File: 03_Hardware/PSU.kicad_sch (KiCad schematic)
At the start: 1 part, among them U301 TPS54202DDC

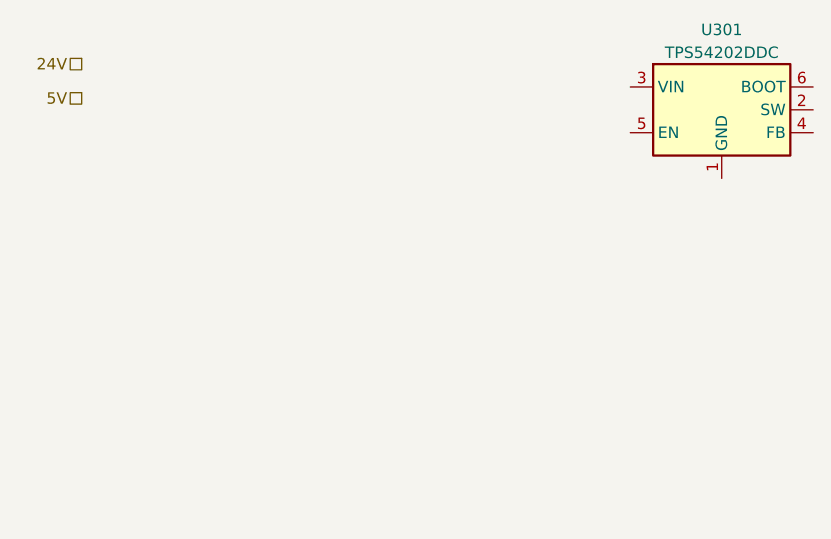
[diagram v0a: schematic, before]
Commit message: Schaltplan erweitert, I2C eingebaut
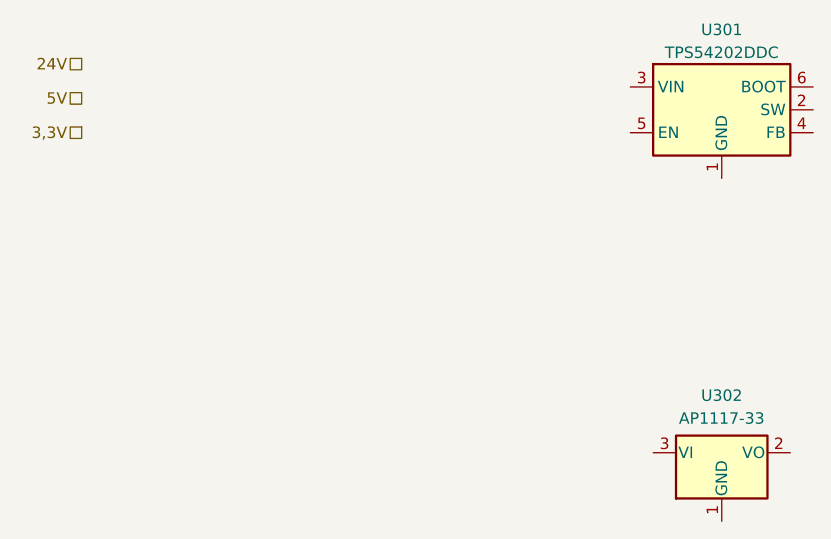
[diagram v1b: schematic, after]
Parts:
- added U302: AP1117-33, Package_TO_SOT_SMD:SOT-223-3_TabPin2, symbol Regulator_Linear:AP1117-33
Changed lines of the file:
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@@
+    (effects (font (size 1.27 1.27)) (justify right))
+  )
+  (hierarchical_label "3,3V" (shape passive) (at 55.88 71.12 180) (fields_autoplaced)
     (effects (font (size 1.27 1.27)) (justify right))
   )
@@
     (pin "6")
   )
+  (symbol (lib_id "Regulator_Linear:AP1117-33") (at 127 106.68 0) (unit 1)
+    (in_bom yes) (on_board yes) (dnp no) (fields_autoplaced)
+    (default_instance (reference "U302") (unit 1) (value "AP1117-33") (footprint "Package_TO_SOT_SMD:SOT-223-3_TabPin2"))
+    (property "Reference" "U302" (id 0) (at 127 100.33 0)
+      (effects (font (size 1.27 1.27)))
+    )
+    (property "Value" "AP1117-33" (id 1) (at 127 102.87 0)
+      (effects (font (size 1.27 1.27)))
+    )
+    (property "Footprint" "Package_TO_SOT_SMD:SOT-223-3_TabPin2" (id 2) (at 127 101.6 0)
+      (effects (font (size 1.27 1.27)) hide)
+    )
+    (property "Datasheet" "http://www.diodes.com/datasheets/AP1117.pdf" (id 3) (at 129.54 113.03 0)
+      (effects (font (size 1.27 1.27)) hide)
+    )
+    (pin "1")
+    (pin "2")
+    (pin "3")
+  )
 )

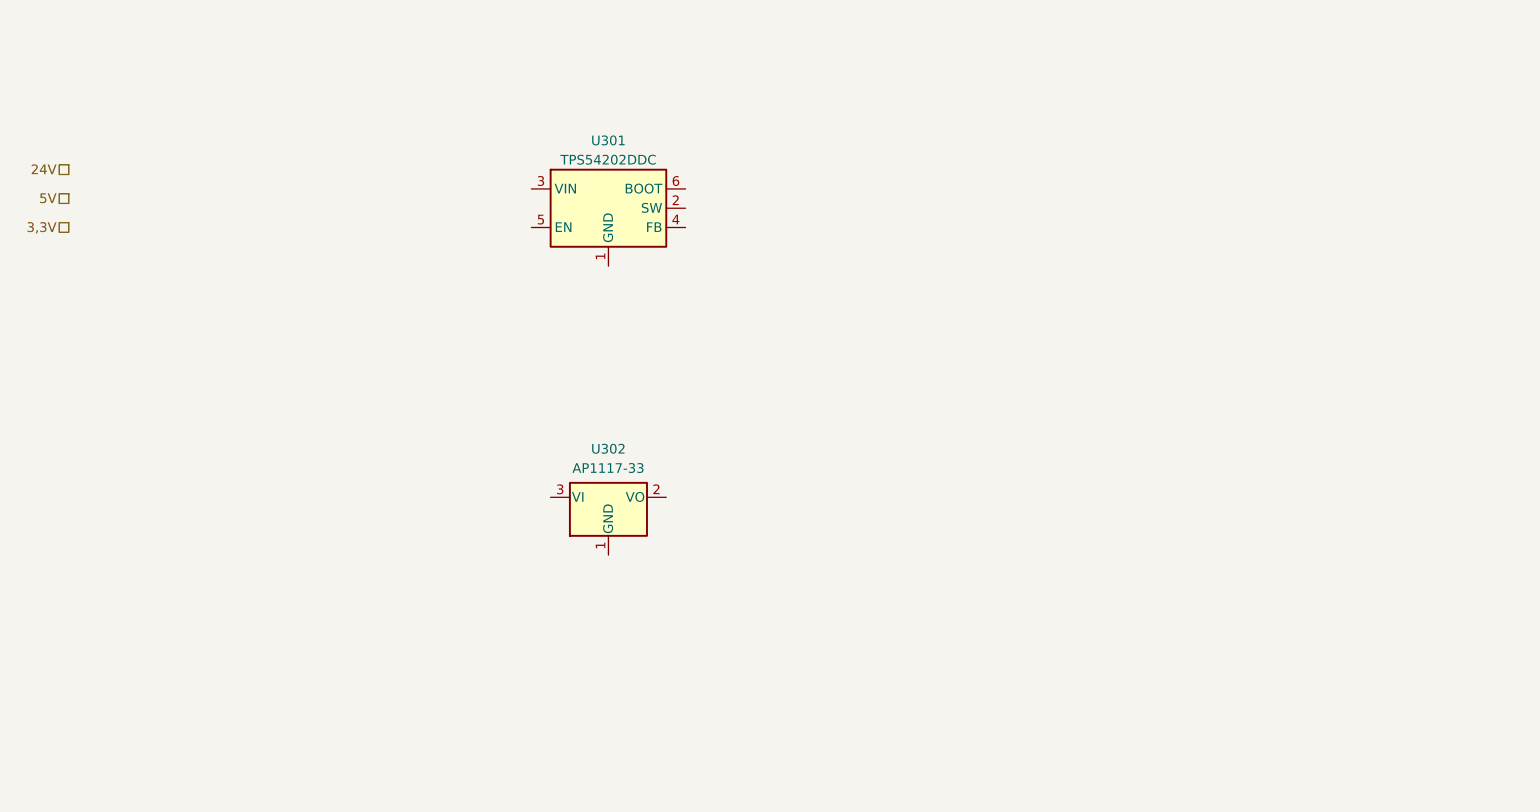
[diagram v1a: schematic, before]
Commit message: Schaltwandler für 5V und Linearwandler für 3,3V angelegt
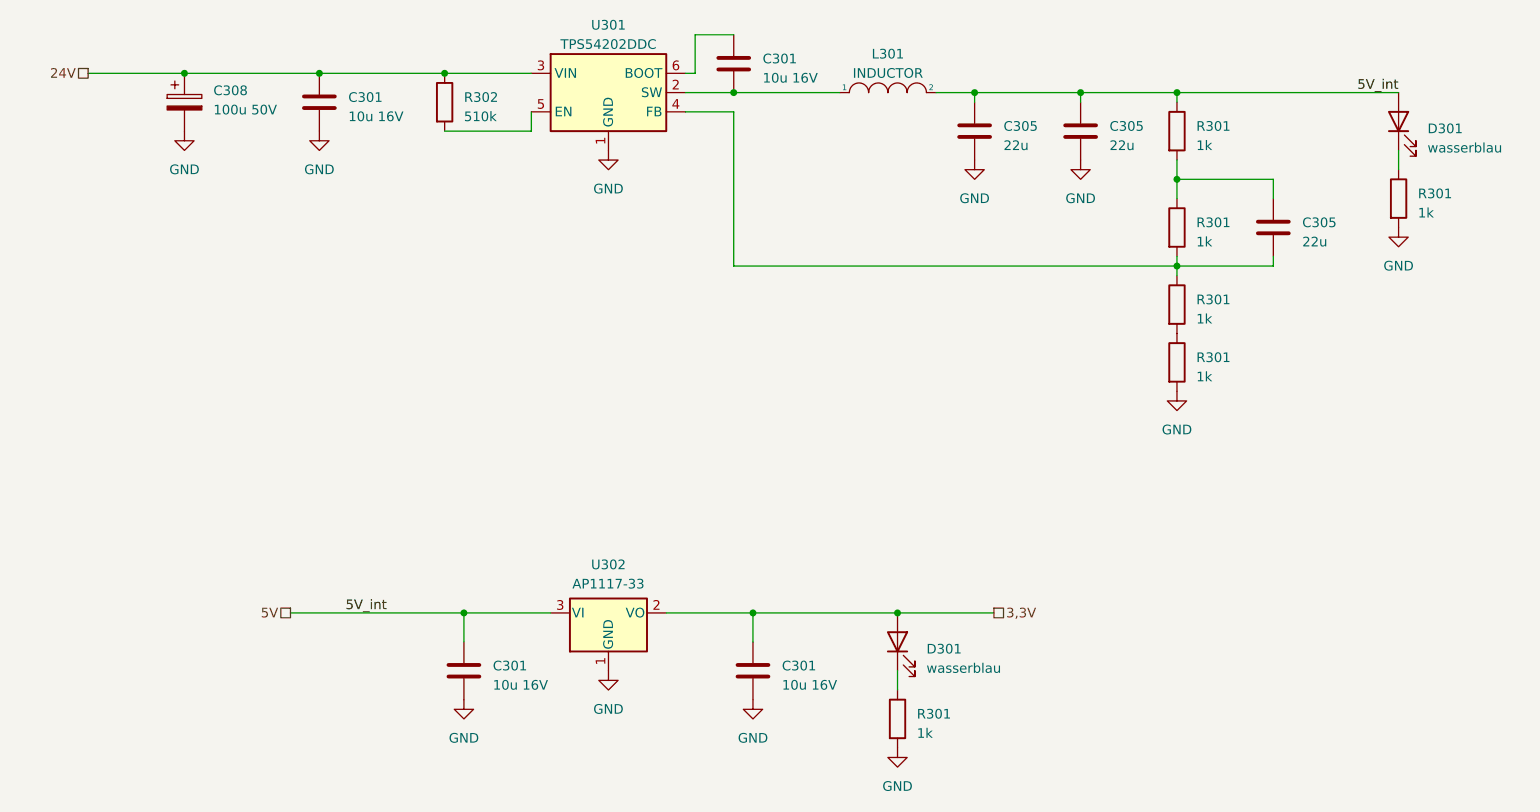
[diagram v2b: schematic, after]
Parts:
- added C301 (x4): 10u 16V, symbol Device:C
- added C305 (x3): 22u, symbol Device:C
- added C308: 100u 50V, symbol Device:C_Polarized
- added D301 (x2): wasserblau, symbol Device:LED
- added L301: INDUCTOR, symbol pspice:INDUCTOR
- added R301 (x6): 1k, symbol Device:R
- added R302: 510k, symbol Device:R
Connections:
- net 24V: now also U301.3 (VIN), C301.1, C308.1, R302.1
- net 3,3V: now also U302.2 (VO), C301.1, D301.2 (A)
- net 5V: now also U302.3 (VI), C301.1, C305.1, C305.1, D301.2 (A), L301.2, R301.1
- net GND: now reaches U301.1 (GND)
- net GND: now also U302.1 (GND), C301.2, C301.2, C301.2, C305.2, C305.2, C308.2, R301.2, R301.2, R301.2
- net at U301.2 (SW): now also C301.2, L301.1
- net at U301.4 (FB): now also C305.2, R301.1, R301.2
- net at U301.5 (EN): now also R302.2
- net at U301.6 (BOOT): now also C301.1
- new net: D301.1 (K), R301.1 (x2)
- new net: R301.1, R301.2
- new net: C305.1, R301.1, R301.2
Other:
- title: Stromversorgung der 5V-Komponenten -> Stromversorgung der 5V und 3,3V-Komponenten
- moved on the sheet: U301, U302

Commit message: Versionsänderungen 6.99 auf 7.0rc, Übergang alte Version 1 auf Version 2.dev
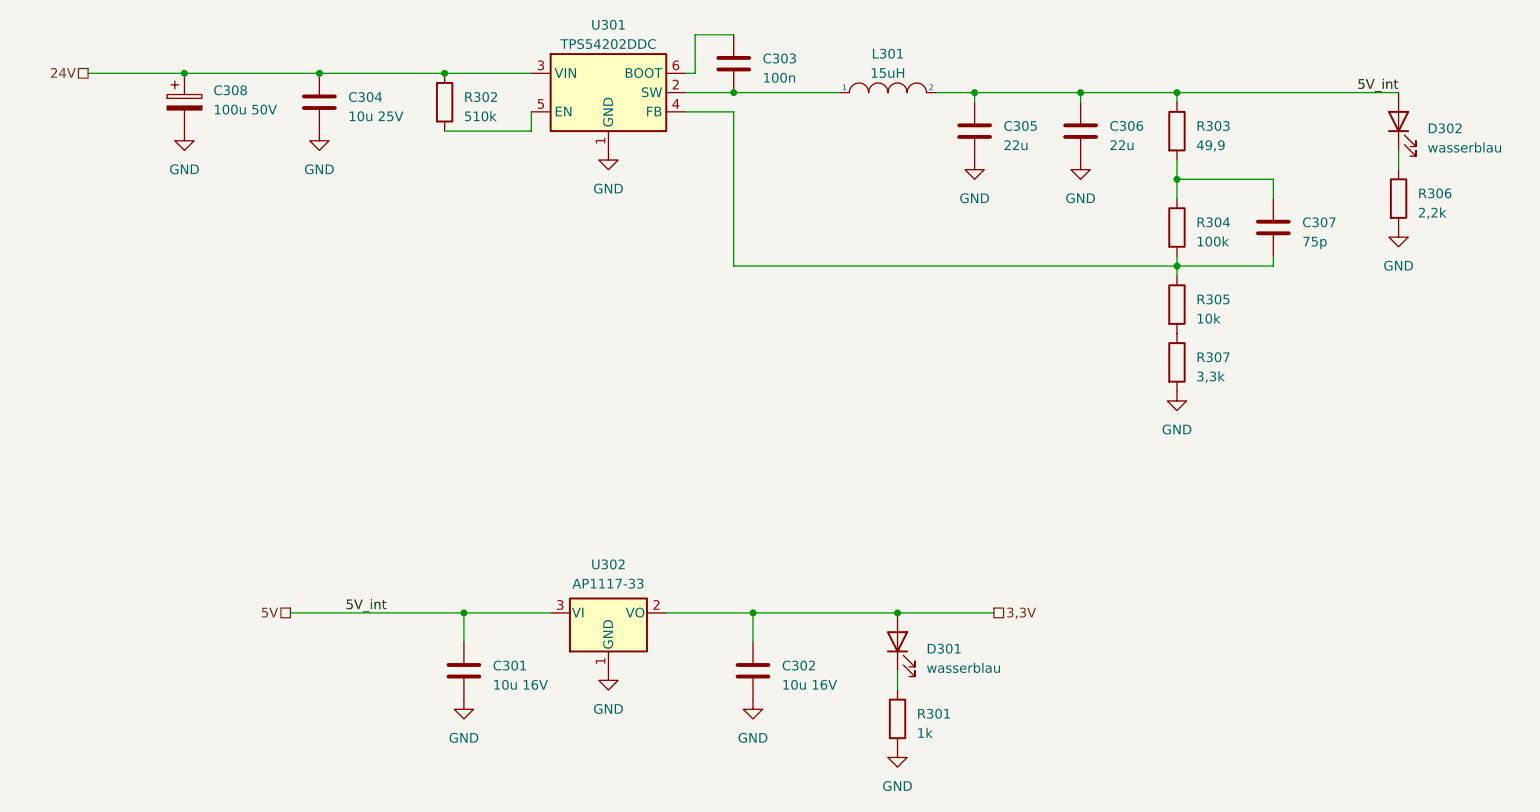
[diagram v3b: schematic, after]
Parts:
- C301, C305: footprint (none) -> Capacitor_SMD:C_1206_3216Metric
- C302: renamed from C301; footprint (none) -> Capacitor_SMD:C_1206_3216Metric
- C303: renamed from C301; value 10u 16V -> 100n; footprint (none) -> Capacitor_SMD:C_0603_1608Metric
- C304: renamed from C301; value 10u 16V -> 10u 25V; footprint (none) -> Capacitor_SMD:C_1206_3216Metric
- C306: renamed from C305; footprint (none) -> Capacitor_SMD:C_1206_3216Metric
- C307: renamed from C305; value 22u -> 75p; footprint (none) -> Capacitor_SMD:C_0603_1608Metric
- C308: footprint (none) -> Capacitor_THT:CP_Radial_D8.0mm_P3.50mm
- D301: footprint (none) -> LED_SMD:LED_0603_1608Metric
- D302: renamed from D301; footprint (none) -> LED_SMD:LED_0603_1608Metric
- L301: value INDUCTOR -> 15uH; footprint (none) -> Inductor_SMD:L_Bourns-SRN4018
- R301, R302: footprint (none) -> Resistor_SMD:R_0603_1608Metric
- R303: renamed from R301; value 1k -> 49,9; footprint (none) -> Resistor_SMD:R_0603_1608Metric
- R304: renamed from R301; value 1k -> 100k; footprint (none) -> Resistor_SMD:R_0603_1608Metric
- R305: renamed from R301; value 1k -> 10k; footprint (none) -> Resistor_SMD:R_0603_1608Metric
- R306: renamed from R301; value 1k -> 2,2k; footprint (none) -> Resistor_SMD:R_0603_1608Metric
- R307: renamed from R301; value 1k -> 3,3k; footprint (none) -> Resistor_SMD:R_0603_1608Metric

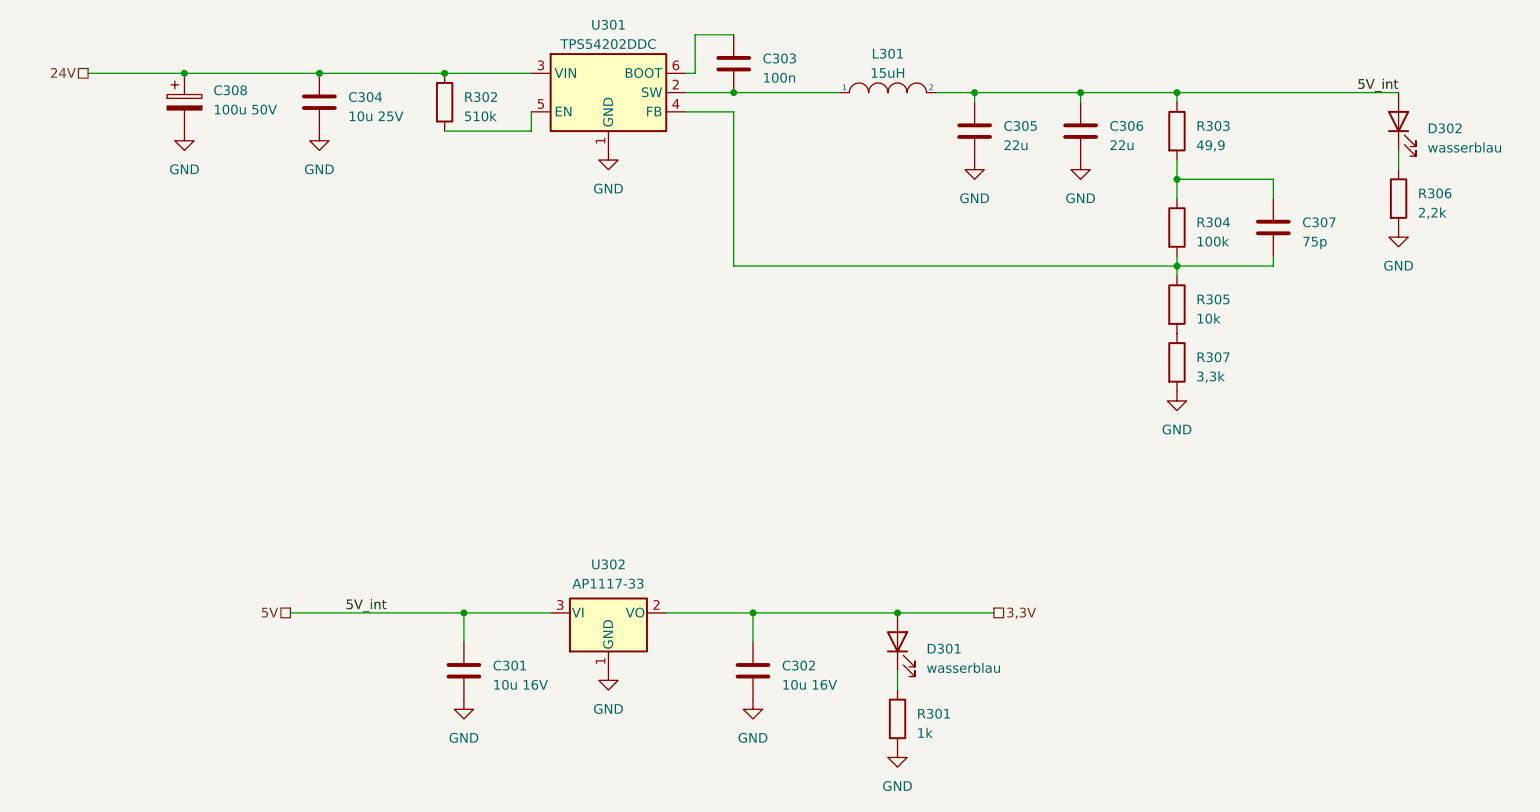
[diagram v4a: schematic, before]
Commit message: Stecker fertig ausgewählt und Layout etwa 60% fertig
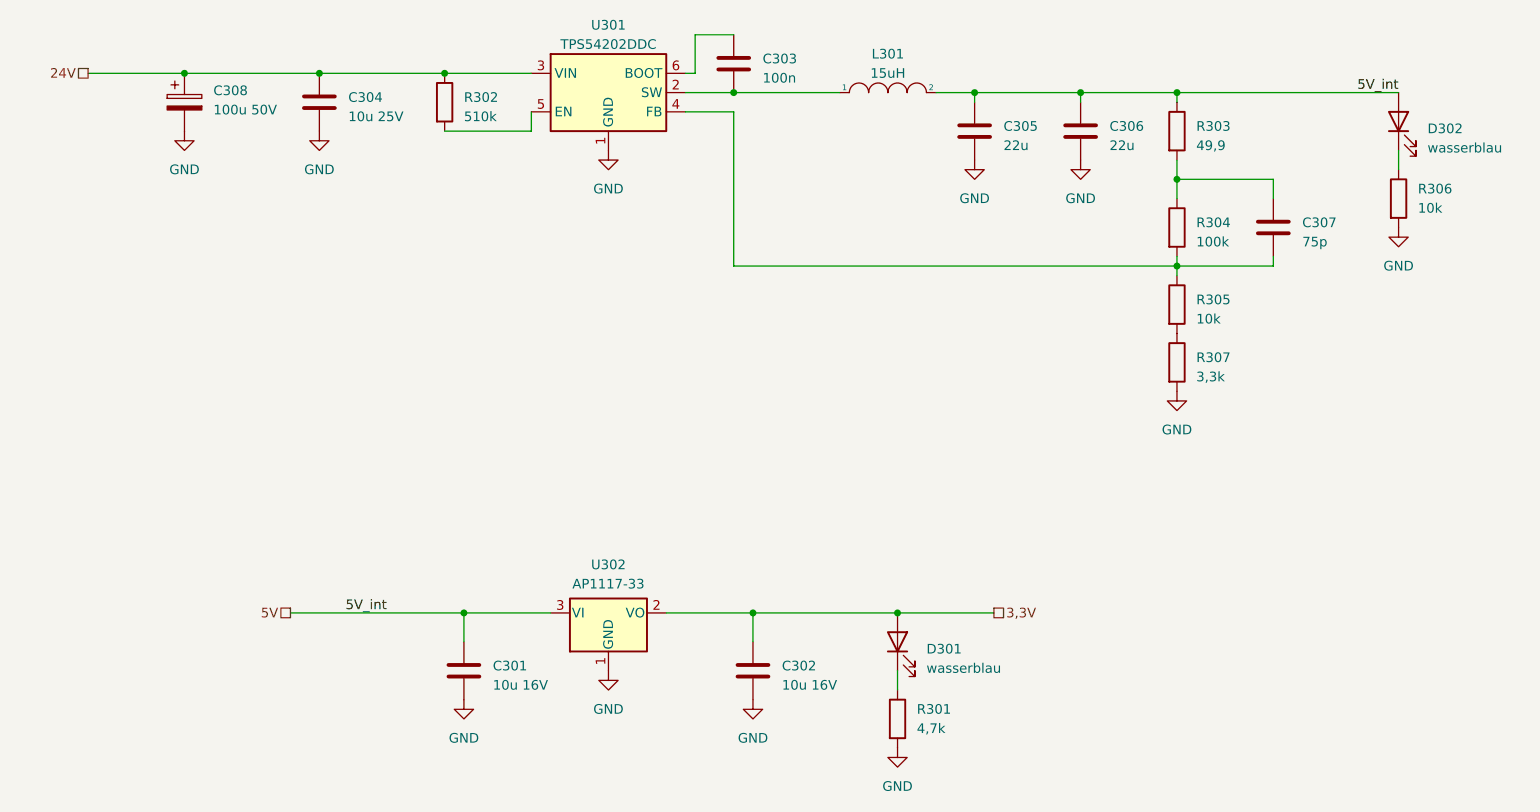
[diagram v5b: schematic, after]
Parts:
- R301: value 1k -> 4,7k
- R306: value 2,2k -> 10k
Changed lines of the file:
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@@
   (symbol (lib_id "Device:R") (at 231.14 67.31 0) (unit 1)
     (in_bom yes) (on_board yes) (dnp no) (fields_autoplaced)
-    (property "Reference" "R306" (at 233.68 66.675 0)
-      (effects (font (size 1.27 1.27)) (justify left))
-    )
-    (property "Value" "2,2k" (at 233.68 69.215 0)
+    (property "Reference" "R306" (at 233.68 66.04 0)
+      (effects (font (size 1.27 1.27)) (justify left))
+    )
+    (property "Value" "10k" (at 233.68 68.58 0)
       (effects (font (size 1.27 1.27)) (justify left))
     )
@@
   (symbol (lib_id "Device:R") (at 165.1 135.89 0) (unit 1)
     (in_bom yes) (on_board yes) (dnp no) (fields_autoplaced)
-    (property "Reference" "R301" (at 167.64 135.255 0)
-      (effects (font (size 1.27 1.27)) (justify left))
-    )
-    (property "Value" "1k" (at 167.64 137.795 0)
-      (effects (font (size 1.27 1.27)) (justify left))
-    )
+    (property "Reference" "R301" (at 167.64 134.62 0)
+      (effects (font (size 1.27 1.27)) (justify left))
+    )
+    (property "Value" "4,7k" (at 167.64 137.16 0)
+      (effects (font (size 1.27 1.27)) (justify left))
+    )
